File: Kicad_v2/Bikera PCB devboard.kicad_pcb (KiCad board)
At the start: 4 copper layers, 60 x 40 mm, 114 parts, among them IC1 DRV5032DULPGM, IC2 BQ25630YBGR, IC3 DRV5032DULPGM, IC4 FM24V01A-G, J1 USB4105-GF-A-060, J3 ST-LINK BTB, J7 Waveshare_ePaper_module, SW1 SW_Reset, SW2 SW_Boot, U1 RT6158HWSC, U2 TCR3UG33A_LF, U3 STM32L431CCTx, U4 TPS61253F, U5 ATECC608B-SSHDA-T, U6 LC76GPAMD, U7 USBLC6-2SC6, U8 SMF05CT1G, U9 RAK11720

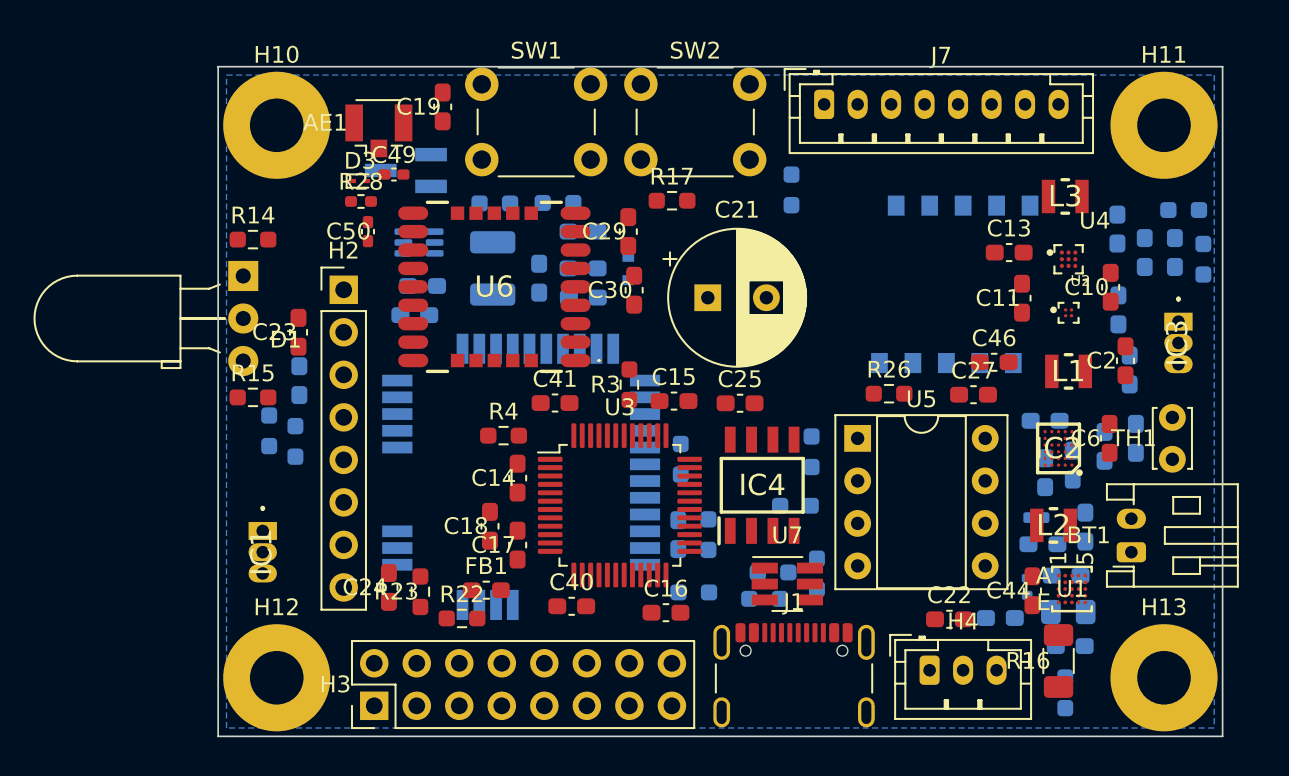
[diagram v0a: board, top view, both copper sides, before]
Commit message: KiCad PCB silkscreen aangepast
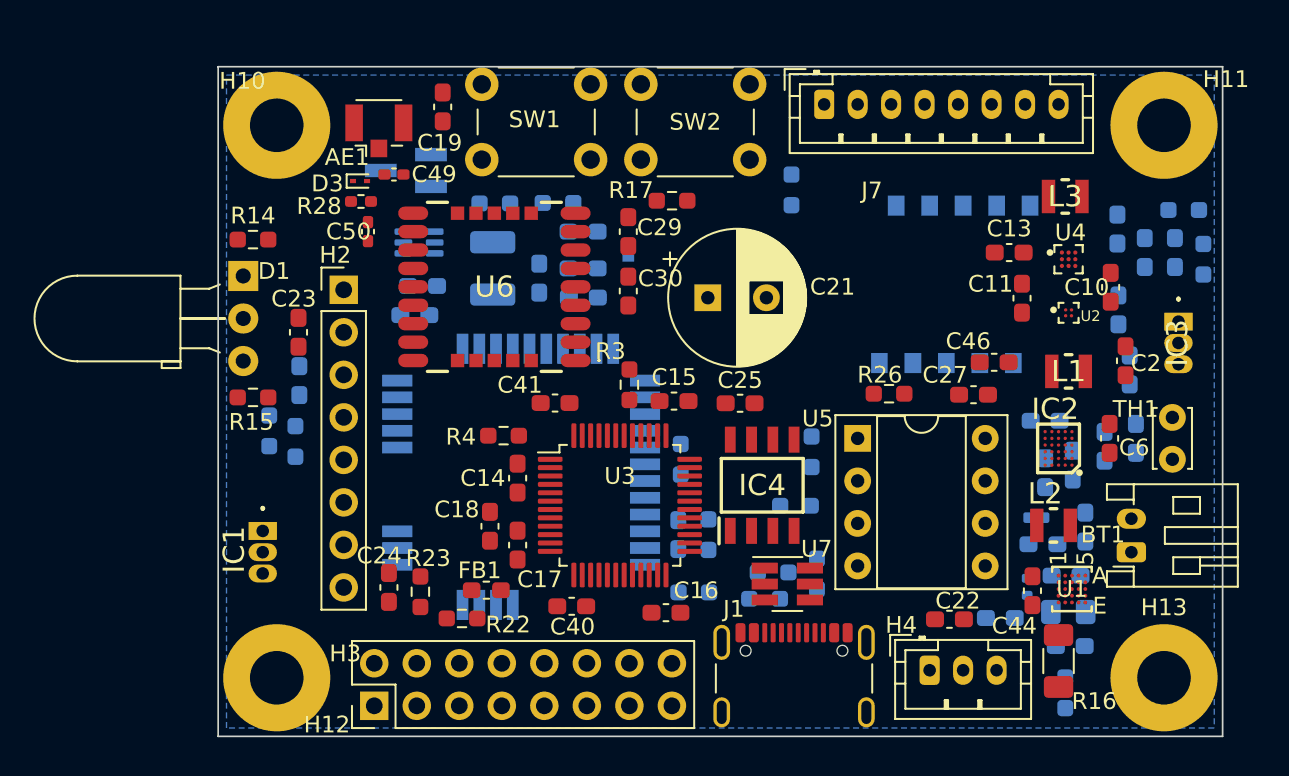
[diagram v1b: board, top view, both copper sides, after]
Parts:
- TH1: value Thermistor_NTC -> NTC
- moved C30 0.35 mm to (24.5, 13.4)
